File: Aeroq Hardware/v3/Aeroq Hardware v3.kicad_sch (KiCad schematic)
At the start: 65 parts, among them Q1 Si1308EDL, U2 ESP32-C3-MINI-1-N4, U3 AMS1117-3.3, U4 SCD40-D-R1

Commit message: Remove lock files and update platformio.ini and main.cpp for ESP32-S3 project
- Deleted lock files for KiCad PCB and schematic to clean up project directory.
- Changed monitor port from COM3 to COM4 in platformio.ini for correct serial communication.
- Modified Serial initialization in main.cpp to include a timeout for better reliability during setup.
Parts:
- removed D5: LED, LED_SMD:LED_0603_1608Metric, symbol Device:LED
- removed R5: 10k, Resistor_SMD:R_0402_1005Metric, symbol Device:R
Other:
- moved on the sheet: C25

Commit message: updates to kicad schematic/pcb
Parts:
- removed CN1: ~, CONN-SMD_5P-P2.00_ZX-PH2.0-WT5P:CONN-SMD_5P-P2.00_ZX-PH2.0-WT5P, symbol Megastar ZX-PH2.0-WT5P:ZX-PH2.0-WT5P
- added U5: ~, JST SM05B-GHS-TB(LF)(SN):CONN-SMD_5P-P1.25_SM05B-GHS-TB-LF-SN, symbol JST SM05B-GHS-TB(LF)(SN):SM05B-GHS-TB(LF)(SN)
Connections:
- net +5V: now also U5.5
- net GND: now also U5.1, U5.4, U5.6, U5.7
- net SCL: now also U5.2
- net SDA: now also U5.3
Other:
- moved on the sheet: C10, C11, R6, R7

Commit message: PCB Updates
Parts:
- D2, D3, D4: footprint SOD-523_L1.2-W0.8-LS1.6-BI:SOD-523_L1.2-W0.8-LS1.6-BI -> Project Footprints:SOD-523_L1.2-W0.8-LS1.6-BI
- FPC1: footprint FPC-SMD_24P-P0.50_FPC-05FB-24PH20:FPC-SMD_24P-P0.50_FPC-05FB-24PH20 -> Project Footprints:FPC-SMD_24P-P0.50_FPC-05FB-24PH20
- SW1, SW2: footprint SW-SMD_L3.9-W3.0-P4.45:SW-SMD_L3.9-W3.0-P4.45 -> Project Footprints:SW-SMD_L3.9-W3.0-P4.45
- U1: footprint USBC_SMD_VERTICAL:TYPE-C-SMD_USB4120-03-C -> Project Footprints:TYPE-C-SMD_USB4120-03-C
- U2: footprint custom_footprints:XCVR_ESP32-C3-MINI-1-N4 -> Project Footprints:XCVR_ESP32-C3-MINI-1-N4
- U4: footprint Sensor:Sensirion_SCD4x-1EP_10.1x10.1mm_P1.25mm_EP4.8x4.8mm -> Project Footprints:XDCR_SCD40-D-R1
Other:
- moved on the sheet: U4
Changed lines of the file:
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@@
 	)
 	(junction
+		(at 213.36 134.62)
+		(diameter 0)
+		(color 0 0 0 0)
+	)
+	(junction
 		(at 38.1 67.31)
 		(diameter 0)
@@
 	)
 	(no_connect
-		(at 179.07 148.59)
+		(at 179.07 147.32)
 	)
 	(wire
@@
 	(wire
 		(pts
-			(xy 175.26 143.51) (xy 179.07 143.51)
+			(xy 177.8 142.24) (xy 179.07 142.24)
 		)
 		(stroke
@@
 	(wire
 		(pts
-			(xy 209.55 135.89) (xy 213.36 135.89)
+			(xy 209.55 134.62) (xy 213.36 134.62)
 		)
 		(stroke
@@
 	(wire
 		(pts
+			(xy 213.36 149.86) (xy 213.36 151.13)
+		)
+		(stroke
+			(width 0)
+			(type default)
+		)
+	)
+	(wire
+		(pts
 			(xy 34.29 39.37) (xy 34.29 15.24)
 		)
@@
 	(wire
 		(pts
-			(xy 213.36 138.43) (xy 209.55 138.43)
+			(xy 213.36 137.16) (xy 209.55 137.16)
 		)
 		(stroke
@@
 	(wire
 		(pts
-			(xy 175.26 140.97) (xy 179.07 140.97)
+			(xy 176.53 139.7) (xy 179.07 139.7)
 		)
 		(stroke
@@
 	(wire
 		(pts
-			(xy 209.55 151.13) (xy 213.36 151.13)
+			(xy 209.55 149.86) (xy 213.36 149.86)
 		)
 		(stroke
@@
 	(wire
 		(pts
+			(xy 177.8 142.24) (xy 177.8 143.51)
+		)
+		(stroke
+			(width 0)
+			(type default)
+		)
+	)
+	(wire
+		(pts
 			(xy 260.35 67.31) (xy 261.62 67.31)
 		)
@@
 	(wire
 		(pts
+			(xy 213.36 134.62) (xy 213.36 135.89)
+		)
+		(stroke
+			(width 0)
+			(type default)
+		)
+	)
+	(wire
+		(pts
 			(xy 231.14 107.95) (xy 231.14 106.68)
 		)
@@
 	(wire
 		(pts
+			(xy 176.53 139.7) (xy 176.53 140.97)
+		)
+		(stroke
+			(width 0)
+			(type default)
+		)
+	)
+	(wire
+		(pts
 			(xy 57.15 175.26) (xy 64.77 175.26)
 		)
@@
 	(wire
 		(pts
+			(xy 176.53 140.97) (xy 175.26 140.97)
+		)
+		(stroke
+			(width 0)
+			(type default)
+		)
+	)
+	(wire
+		(pts
 			(xy 109.22 176.53) (xy 130.81 176.53)
 		)
@@
 	(wire
 		(pts
-			(xy 213.36 133.35) (xy 213.36 135.89)
+			(xy 213.36 133.35) (xy 213.36 134.62)
 		)
 		(stroke
@@
 	(wire
 		(pts
-			(xy 213.36 135.89) (xy 213.36 138.43)
+			(xy 213.36 135.89) (xy 213.36 137.16)
 		)
 		(stroke
@@
 	(wire
 		(pts
+			(xy 177.8 143.51) (xy 175.26 143.51)
+		)
+		(stroke
+			(width 0)
+			(type default)
+		)
+	)
+	(wire
+		(pts
 			(xy 138.43 176.53) (xy 147.32 176.53)
 		)
@@
 			)
 		)
-		(property "Footprint" "SW-SMD_L3.9-W3.0-P4.45:SW-SMD_L3.9-W3.0-P4.45"
+		(property "Footprint" "Project Footprints:SW-SMD_L3.9-W3.0-P4.45"
 			(at 135.89 72.39 0)
 			(effects
@@
 			)
 		)
-		(property "Footprint" "SOD-523_L1.2-W0.8-LS1.6-BI:SOD-523_L1.2-W0.8-LS1.6-BI"
+		(property "Footprint" "Project Footprints:SOD-523_L1.2-W0.8-LS1.6-BI"
 			(at 90.17 59.69 0)
 			(effects
@@
 			)
 		)
-		(property "Footprint" "USBC_SMD_VERTICAL:TYPE-C-SMD_USB4120-03-C"
+		(property "Footprint" "Project Footprints:TYPE-C-SMD_USB4120-03-C"
 			(at 52.07 46.99 0)
 			(effects
@@
 			)
 		)
-		(property "Footprint" "SOD-523_L1.2-W0.8-LS1.6-BI:SOD-523_L1.2-W0.8-LS1.6-BI"
+		(property "Footprint" "Project Footprints:SOD-523_L1.2-W0.8-LS1.6-BI"
 			(at 82.55 59.69 0)
 			(effects
@@
 			)
 		)
-		(property "Footprint" "SOD-523_L1.2-W0.8-LS1.6-BI:SOD-523_L1.2-W0.8-LS1.6-BI"
+		(property "Footprint" "Project Footprints:SOD-523_L1.2-W0.8-LS1.6-BI"
 			(at 96.52 59.69 0)
 			(effects
@@
 			)
 		)
-		(property "Footprint" "SW-SMD_L3.9-W3.0-P4.45:SW-SMD_L3.9-W3.0-P4.45"
+		(property "Footprint" "Project Footprints:SW-SMD_L3.9-W3.0-P4.45"
 			(at 135.89 34.29 0)
 			(effects
@@
 			)
 		)
-		(property "Footprint" "custom_footprints:XCVR_ESP32-C3-MINI-1-N4"
+		(property "Footprint" "Project Footprints:XCVR_ESP32-C3-MINI-1-N4"
 			(at 242.57 64.77 0)
 			(effects
@@
 	(symbol
 		(lib_id "SCD40-D-R1:SCD40-D-R1")
-		(at 194.31 143.51 0)
+		(at 194.31 142.24 0)
 		(unit 1)
 		(exclude_from_sim no)
@@
 		(fields_autoplaced yes)
 		(property "Reference" "U4"
-			(at 194.31 128.27 0)
+			(at 194.31 127 0)
 			(effects
 				(font
@@
 		)
 		(property "Value" "SCD40-D-R1"
-			(at 194.31 130.81 0)
+			(at 194.31 129.54 0)
 			(effects
 				(font
@@
 			)
 		)
-		(property "Footprint" "Sensor:Sensirion_SCD4x-1EP_10.1x10.1mm_P1.25mm_EP4.8x4.8mm"
-			(at 194.31 143.51 0)
+		(property "Footprint" "Project Footprints:XDCR_SCD40-D-R1"
+			(at 194.31 142.24 0)
 			(effects
 				(font
@@
 		)
 		(property "Datasheet" ""
-			(at 194.31 143.51 0)
+			(at 194.31 142.24 0)
 			(effects
 				(font
@@
 		)
 		(property "Description" ""
-			(at 194.31 143.51 0)
+			(at 194.31 142.24 0)
 			(effects
 				(font
@@
 		)
 		(property "MF" "Sensirion AG"
-			(at 194.31 143.51 0)
+			(at 194.31 142.24 0)
 			(effects
 				(font
@@
 		)
 		(property "MAXIMUM_PACKAGE_HEIGHT" "6.8mm"
-			(at 194.31 143.51 0)
+			(at 194.31 142.24 0)
 			(effects
 				(font
@@
 		)
 		(property "Package" "None"
-			(at 194.31 143.51 0)
+			(at 194.31 142.24 0)
 			(effects
 				(font
@@
 		)
 		(property "Price" "None"
-			(at 194.31 143.51 0)
+			(at 194.31 142.24 0)
 			(effects
 				(font
@@
 		)
 		(property "Check_prices" "https://www.snapeda.com/parts/SCD40-D-R1/Sensirion/view-part/?ref=eda"
-			(at 194.31 143.51 0)
+			(at 194.31 142.24 0)
 			(effects
 				(font
@@
 		)
 		(property "STANDARD" "Manufacturer Recommendations"
-			(at 194.31 143.51 0)
+			(at 194.31 142.24 0)
 			(effects
 				(font
@@
 		)
 		(property "PARTREV" "1.2"
-			(at 194.31 143.51 0)
+			(at 194.31 142.24 0)
 			(effects
 				(font
@@
 		)
 		(property "SnapEDA_Link" "https://www.snapeda.com/parts/SCD40-D-R1/Sensirion/view-part/?ref=snap"
-			(at 194.31 143.51 0)
+			(at 194.31 142.24 0)
 			(effects
 				(font
@@
 		)
 		(property "MP" "SCD40-D-R1"
-			(at 194.31 143.51 0)
+			(at 194.31 142.24 0)
 			(effects
 				(font
@@
 		)
 		(property "Description_1" "Carbon Dioxide (CO2), Humidity, Temperature Sensor I2C"
-			(at 194.31 143.51 0)
+			(at 194.31 142.24 0)
 			(effects
 				(font
@@
 		)
 		(property "SNAPEDA_PN" "SCD41-D-R2"
-			(at 194.31 143.51 0)
+			(at 194.31 142.24 0)
 			(effects
 				(font
@@
 		)
 		(property "Availability" "In Stock"
-			(at 194.31 143.51 0)
+			(at 194.31 142.24 0)
 			(effects
 				(font
@@
 		)
 		(property "MANUFACTURER" "Sensirion"
-			(at 194.31 143.51 0)
+			(at 194.31 142.24 0)
 			(effects
 				(font
@@
 			)
 		)
-		(property "Footprint" "FPC-SMD_24P-P0.50_FPC-05FB-24PH20:FPC-SMD_24P-P0.50_FPC-05FB-24PH20"
+		(property "Footprint" "Project Footprints:FPC-SMD_24P-P0.50_FPC-05FB-24PH20"
 			(at 152.4 160.02 0)
 			(effects

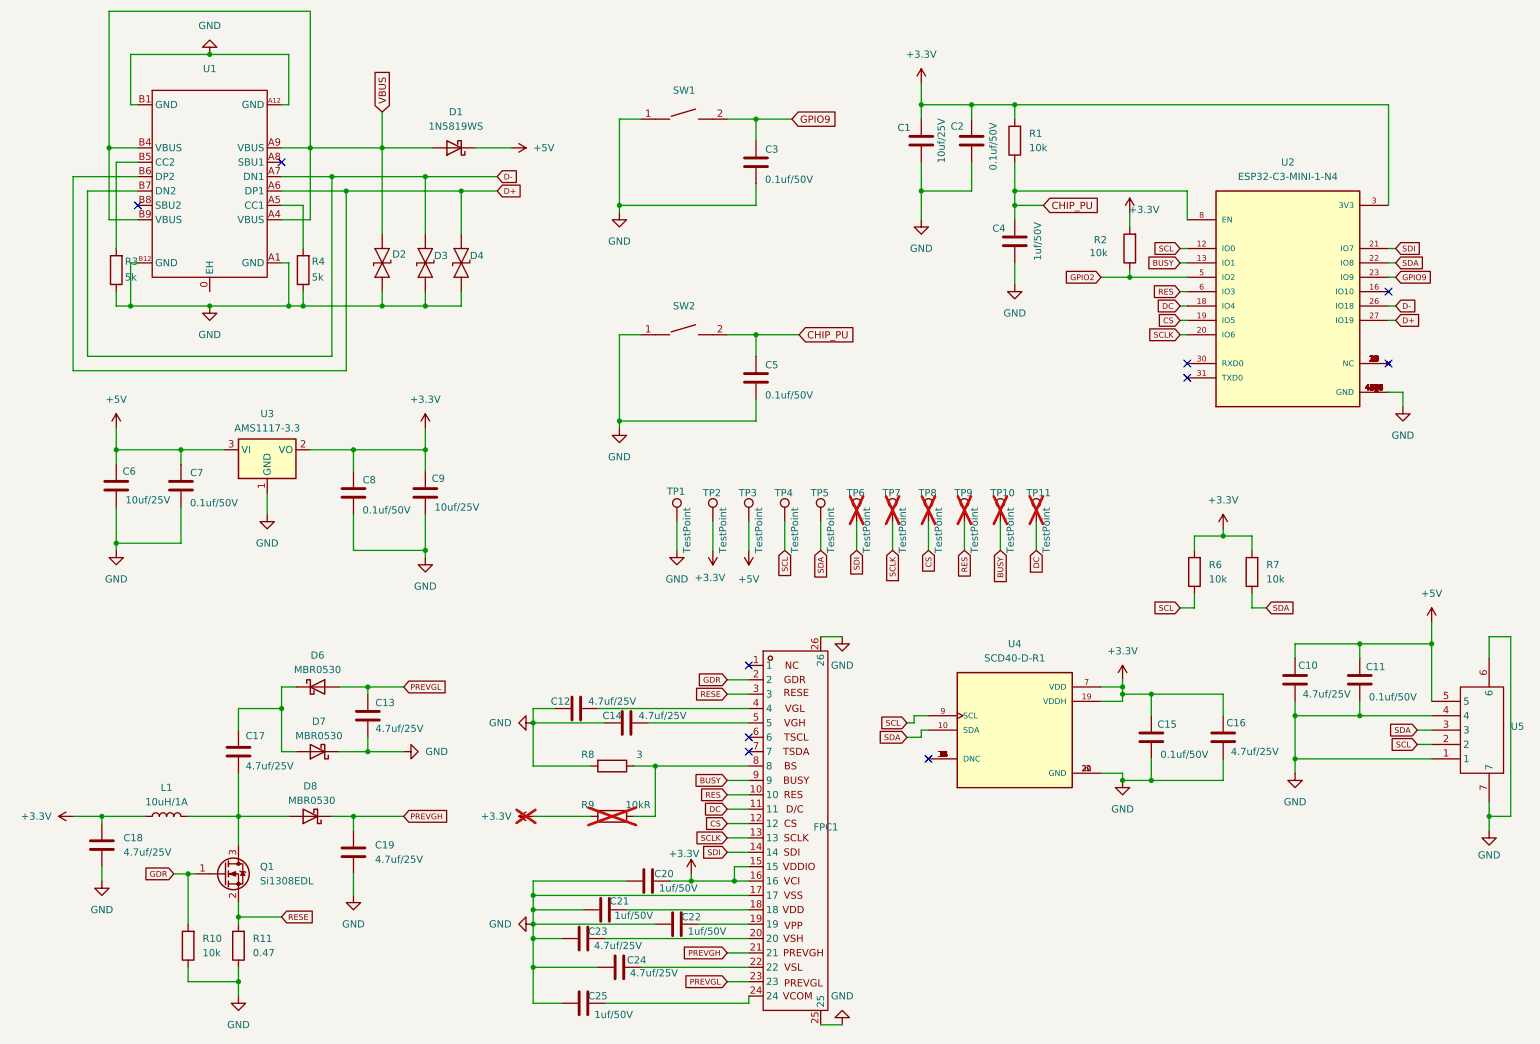
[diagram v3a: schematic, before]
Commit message: KiCad schematic and PCB updates
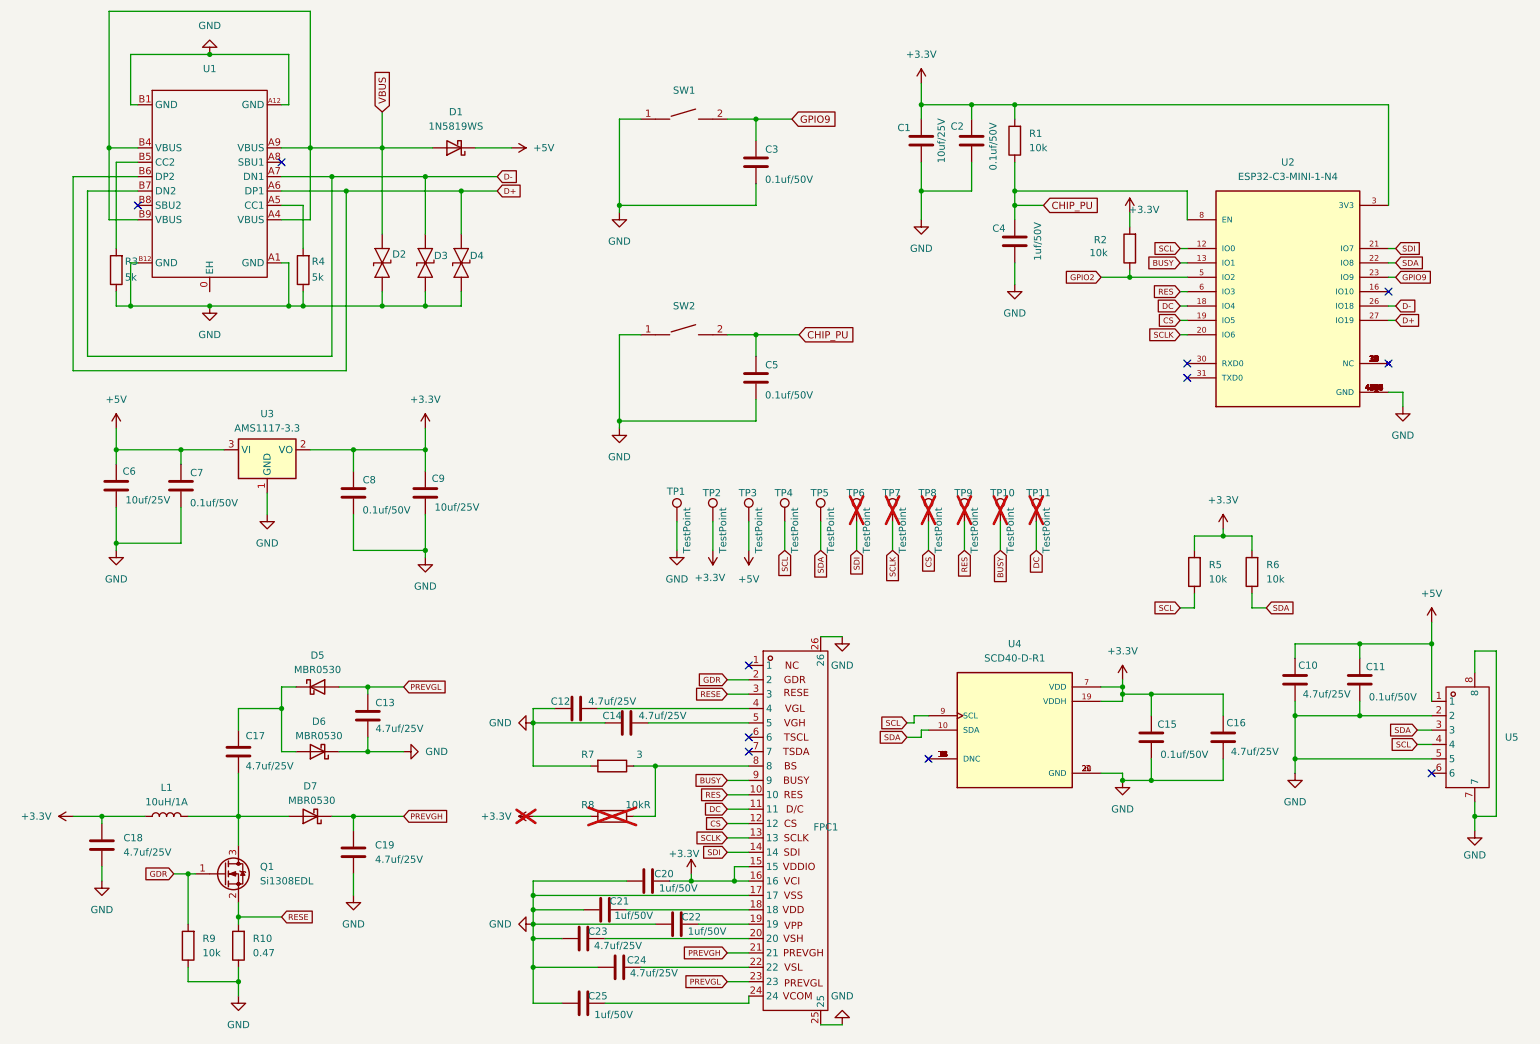
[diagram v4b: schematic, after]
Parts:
- removed U5: ~, JST SM05B-GHS-TB(LF)(SN):CONN-SMD_5P-P1.25_SM05B-GHS-TB-LF-SN, symbol JST SM05B-GHS-TB(LF)(SN):SM05B-GHS-TB(LF)(SN)
- added U5: ~, XUNPU WAFER-GH1.25-6PWB:CONN-SMD_6P-P1.25_XUNPU_WAFER-GH1.25-6PWB, symbol XUNPU WAFER-GH1.25-6PWB:WAFER-GH1.25-6PWB
- renumbered D6 to D5, D7 to D6, D8 to D7, R11 to R10, R6 to R5, R7 to R6, R8 to R7, R9 to R8, R10 to R9
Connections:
- net +5V: now also U5.1
- net GND: now also U5.2, U5.5, U5.7, U5.8
- net SCL: now also U5.4
- net SDA: now also U5.3
- no-connect marks 10 -> 11

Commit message: add my customizations
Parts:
- removed C1, C6, C9: 10uf/25V, Capacitor_SMD:C_0603_1608Metric, symbol Device:C
- removed C10, C12, C13, C14, C16, C17, C18, C19, C23, C24: 4.7uf/25V, Capacitor_SMD:C_0603_1608Metric, symbol Device:C
- removed C11, C15, C2, C3, C5, C7, C8: 0.1uf/50V, Capacitor_SMD:C_0603_1608Metric, symbol Device:C
- removed C20, C21, C22, C25, C4: 1uf/50V, Capacitor_SMD:C_0603_1608Metric, symbol Device:C
- removed D1: 1N5819WS, Diode_SMD:D_SOD-323, symbol Diode:1N5819WS
- removed D2, D3, D4: ~, Project Footprints:SOD-523_L1.2-W0.8-LS1.6-BI, symbol LRC LESD5D5.0CT1G:LESD5D5.0CT1G
- removed D5, D6, D7: MBR0530, Diode_SMD:D_SOD-123, symbol Diode:MBR0530
- removed FPC1: ~, Project Footprints:FPC-SMD_24P-P0.50_FPC-05FB-24PH20, symbol FPC-05FB-24PH20:FPC-05FB-24PH20
- removed L1: 10uH/1A, Inductor_SMD:L_1210_3225Metric, symbol Device:L
- removed Q1: Si1308EDL, Package_TO_SOT_SMD:SOT-323_SC-70, symbol Transistor_FET:Si1308EDL
- removed R1, R2, R5, R6, R9: 10k, Resistor_SMD:R_0402_1005Metric, symbol Device:R
- removed R10: 0.47, Resistor_SMD:R_0402_1005Metric, symbol Device:R
- removed R3, R4: 5k, Resistor_SMD:R_0402_1005Metric, symbol Device:R
- removed R7: 3, Resistor_SMD:R_0402_1005Metric, symbol Device:R
- removed R8: 10kR, Resistor_SMD:R_0402_1005Metric, symbol Device:R
- removed SW1, SW2: ~, Project Footprints:SW-SMD_L3.9-W3.0-P4.45, symbol XUNPU TS-1088-AR02016:TS-1088-AR02016
- removed TP1, TP10, TP11, TP2, TP3, TP4, TP5, TP6, TP7, TP8, TP9: TestPoint, TestPoint:TestPoint_Pad_D1.5mm, symbol Connector:TestPoint
- removed U1: ~, Project Footprints:TYPE-C-SMD_USB4120-03-C, symbol TYPE-C 16PLT-H10:TYPE-C 16PLT-H10.0
- removed U2: ESP32-C3-MINI-1-N4, Project Footprints:XCVR_ESP32-C3-MINI-1-N4, symbol ESP32-C3-MINI-1-N4:ESP32-C3-MINI-1-N4
- removed U3: AMS1117-3.3, Package_TO_SOT_SMD:SOT-223-3_TabPin2, symbol Regulator_Linear:AMS1117-3.3
- removed U4: SCD40-D-R1, Project Footprints:XDCR_SCD40-D-R1, symbol SCD40-D-R1:SCD40-D-R1
- removed U5: ~, XUNPU WAFER-GH1.25-6PWB:CONN-SMD_6P-P1.25_XUNPU_WAFER-GH1.25-6PWB, symbol XUNPU WAFER-GH1.25-6PWB:WAFER-GH1.25-6PWB
- added FID1, FID2, FID3: Fiducial, Fiducial:Fiducial_0.5mm_Mask1.5mm, symbol 2s_mechanical:Fiducial 0.5 / 1.5
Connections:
- no-connect marks 11 -> 0
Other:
- added sheet Display (display.kicad_sch)
- added sheet Microcontroller (microcontroller.kicad_sch)
- added sheet Power (power.kicad_sch)
- added sheet Sensors (sensors.kicad_sch)
- added sheet USB-C (usb-c.kicad_sch)
